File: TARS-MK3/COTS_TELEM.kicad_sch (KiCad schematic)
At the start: 18 parts, among them J1 Conn_02x12_Odd_Even, J2 Conn_02x12_Odd_Even, J3 Conn_02x12_Odd_Even, J4 Conn_02x12_Odd_Even, J5 Conn_01x05_Male, U1 RFM96W-433S2, U2 Feather_M0_RFM96, X1 uFL/SMA

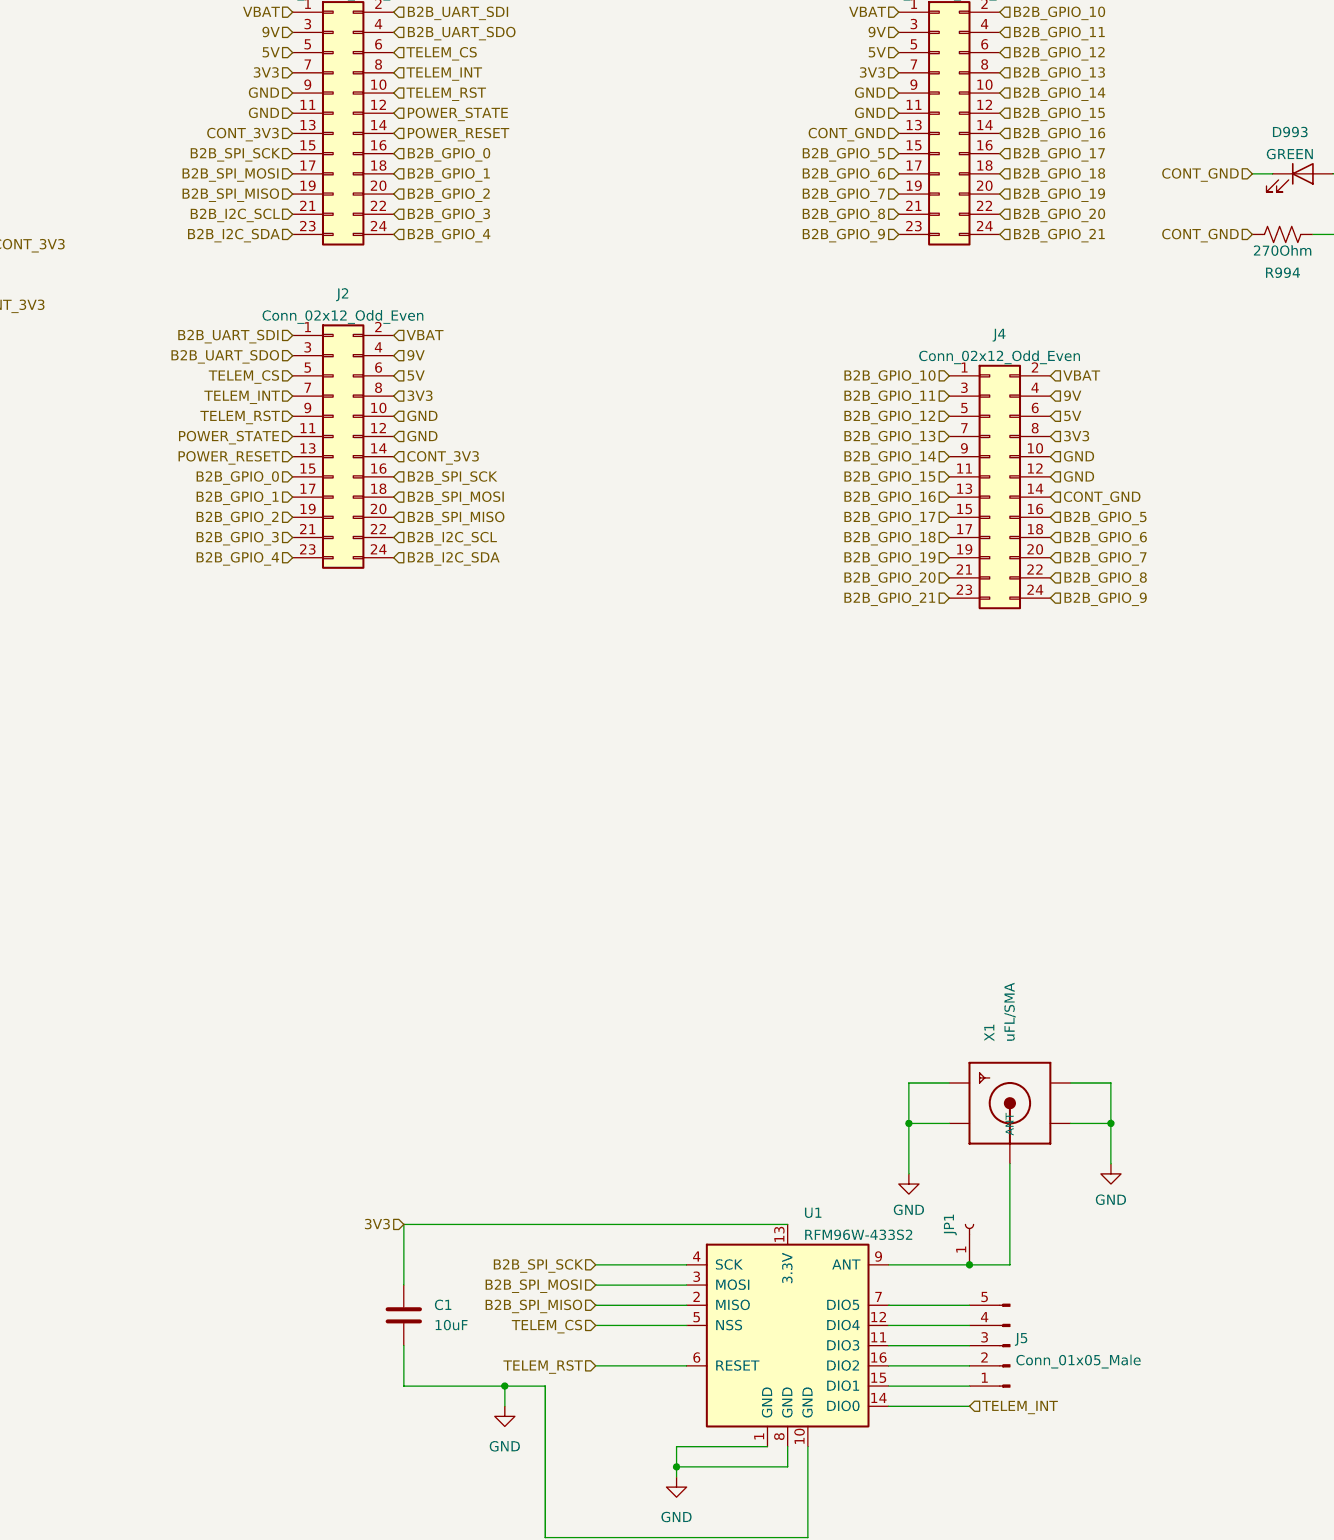
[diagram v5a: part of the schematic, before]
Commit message: allocated telemetry b2b and added battery connector
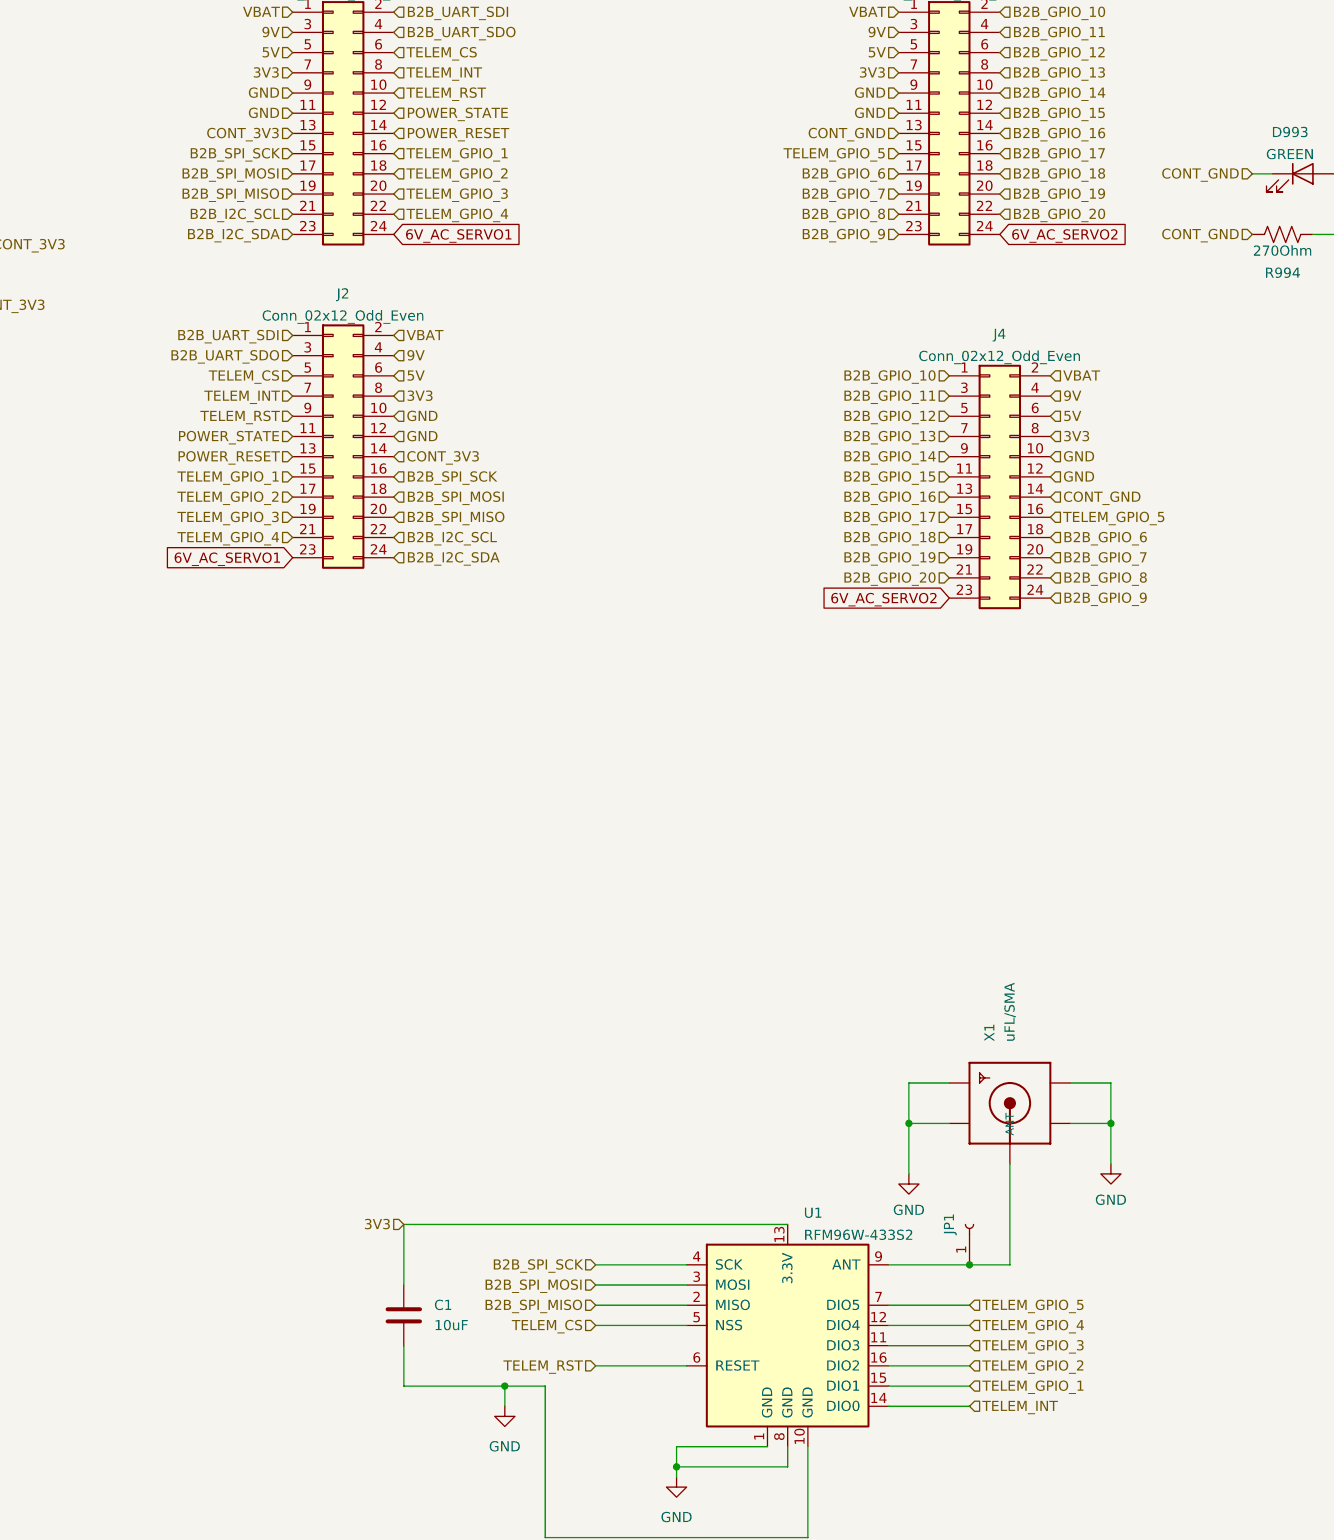
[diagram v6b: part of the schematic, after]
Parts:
- removed J5: Conn_01x05_Male, Connector_PinHeader_2.54mm:PinHeader_1x05_P2.54mm_Vertical, symbol Connector:Conn_01x05_Male
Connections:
- net B2B_GPIO_0 is gone; now on net TELEM_GPIO_1: J1.16 (Pin_16), J2.15 (Pin_15)
- net B2B_GPIO_1 is gone; now on net TELEM_GPIO_2: J1.18 (Pin_18), J2.17 (Pin_17)
- net B2B_GPIO_2 is gone; now on net TELEM_GPIO_3: J1.20 (Pin_20), J2.19 (Pin_19)
- net B2B_GPIO_3 is gone; now on net TELEM_GPIO_4: J1.22 (Pin_22), J2.21 (Pin_21)
- net B2B_GPIO_5 is gone; now on net TELEM_GPIO_5: J3.15 (Pin_15), J4.16 (Pin_16)
- net TELEM_GPIO_1: now reaches U1.15 (DIO1)
- net TELEM_GPIO_2: now reaches U1.16 (DIO2)
- net TELEM_GPIO_3: now reaches U1.11 (DIO3)
- net TELEM_GPIO_4: now reaches U1.12 (DIO4)
- net TELEM_GPIO_5: now reaches U1.7 (DIO5)
- net B2B_GPIO_21 renamed 6V_AC_SERVO2
- net B2B_GPIO_4 renamed 6V_AC_SERVO1

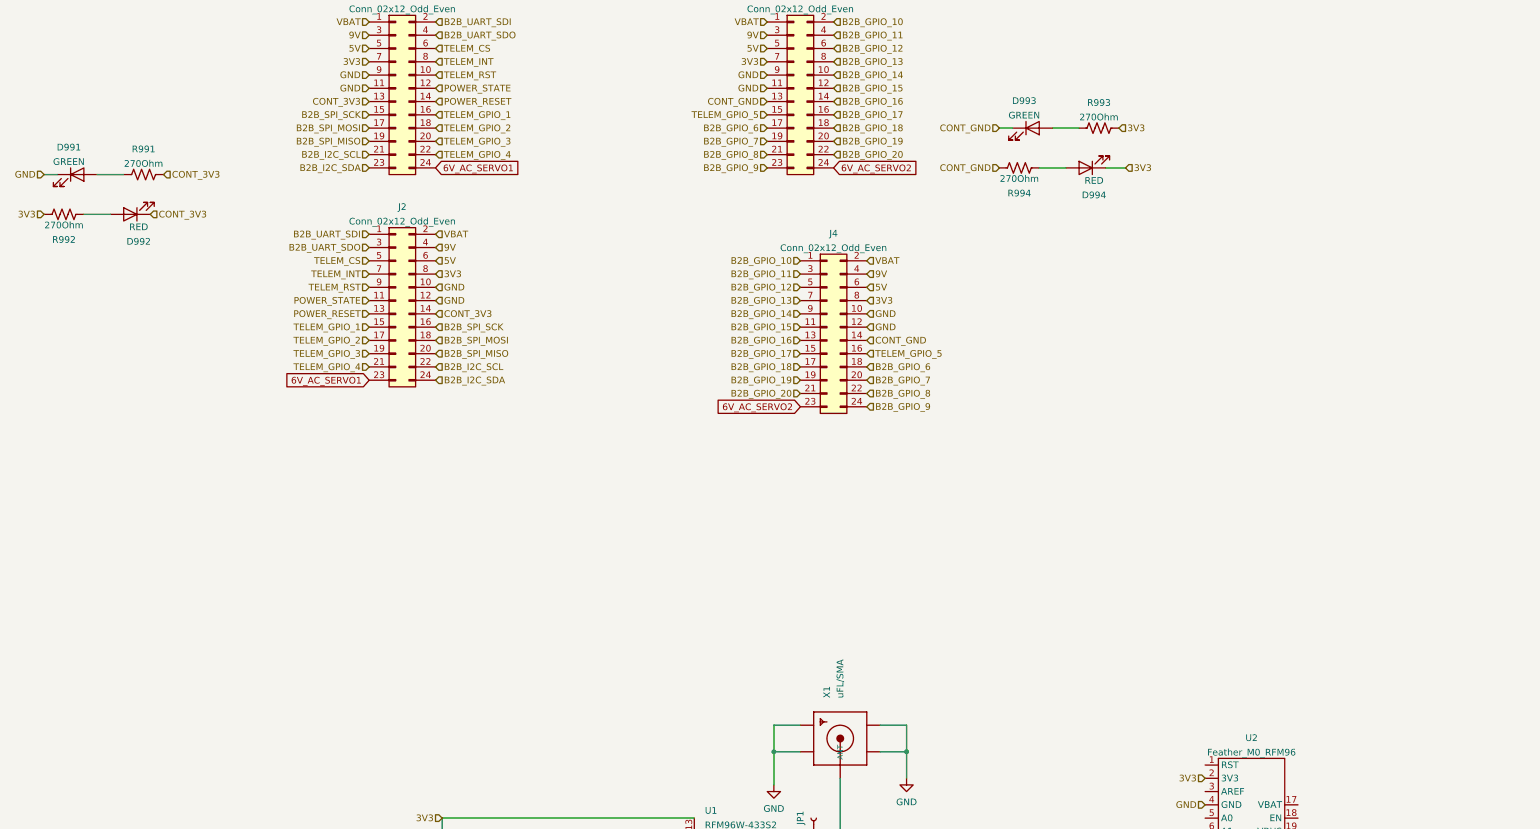
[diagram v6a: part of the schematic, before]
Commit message: moved connectors to top
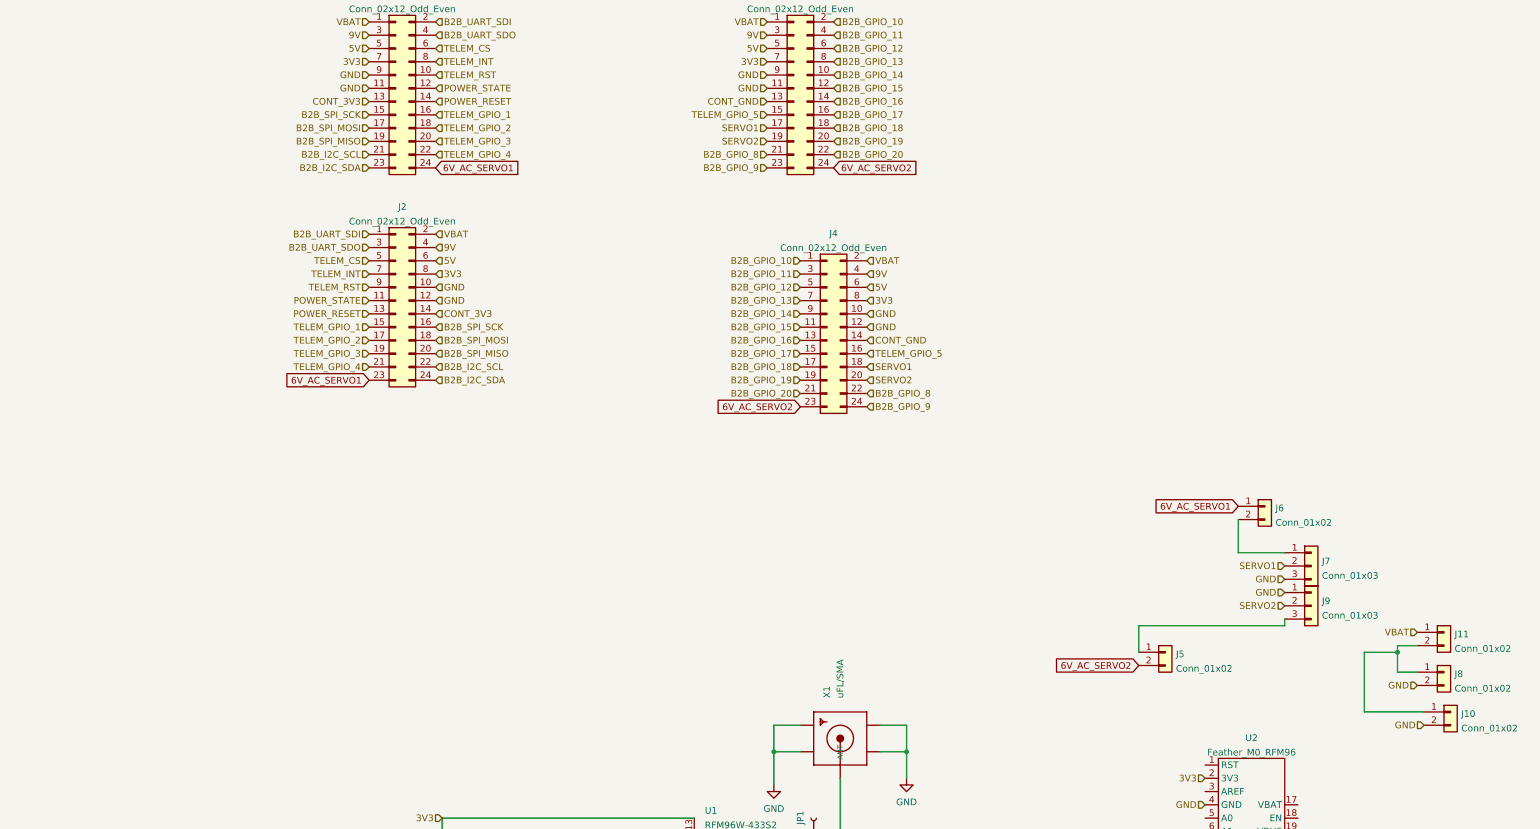
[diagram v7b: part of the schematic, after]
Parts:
- removed D991, D993: GREEN, LED_SMD:LED_0805_2012Metric, symbol D24V50F5:LED
- removed D992, D994: RED, LED_SMD:LED_0805_2012Metric, symbol D24V50F5:LED
- removed R991, R992, R993, R994: 270Ohm, Resistor_SMD:R_0805_2012Metric, symbol D24V50F5:R_US
- added J10, J8: Conn_01x02, Connector_Molex:Molex_Micro-Fit_3.0_43650-0200_1x02_P3.00mm_Horizontal, symbol Connector_Generic:Conn_01x02
- added J11, J5, J6: Conn_01x02, Connector_Molex:Molex_CLIK-Mate_502443-0270_1x02-1MP_P2.00mm_Vertical, symbol Connector_Generic:Conn_01x02
- added J7, J9: Conn_01x03, Connector_Molex:Molex_Micro-Fit_3.0_43650-0300_1x03_P3.00mm_Horizontal, symbol Connector_Generic:Conn_01x03
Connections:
- net 6V_AC_SERVO1: now also J6.1 (Pin_1)
- net 6V_AC_SERVO2: now also J5.2 (Pin_2)
- net GND: now also J10.2 (Pin_2), J7.3 (Pin_3), J8.2 (Pin_2), J9.1 (Pin_1)
- net VBAT: now also J11.1 (Pin_1)
- net B2B_GPIO_6 renamed SERVO1
- net SERVO1: now also J7.2 (Pin_2)
- net B2B_GPIO_7 renamed SERVO2
- net SERVO2: now also J9.2 (Pin_2)
- new net: J6.2 (Pin_2), J7.1 (Pin_1)
- new net: J10.1 (Pin_1), J11.2 (Pin_2), J8.1 (Pin_1)
- new net: J5.1 (Pin_1), J9.3 (Pin_3)

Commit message: stuff
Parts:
- removed J5, J6: Conn_01x02, Connector_Molex:Molex_CLIK-Mate_502443-0270_1x02-1MP_P2.00mm_Vertical, symbol Connector_Generic:Conn_01x02
- J11: footprint Connector_Molex:Molex_CLIK-Mate_502443-0270_1x02-1MP_P2.00mm_Vertical -> Connector_Molex:Molex_CLIK-Mate_502494-0270_1x02-1MP_P2.00mm_Horizontal
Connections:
- net 6V_AC_SERVO1: now also J7.1 (Pin_1)
- net 6V_AC_SERVO2: now also J9.3 (Pin_3)
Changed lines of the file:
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@@
-    (stroke (width 0) (type default) (color 0 0 0 0))
-  )
-  (wire (pts (xy 185.42 44.45) (xy 185.42 39.37))
     (stroke (width 0) (type default) (color 0 0 0 0))
   )
@@
     (stroke (width 0) (type default) (color 0 0 0 0))
   )
-  (wire (pts (xy 204.47 19.05) (xy 204.47 25.4))
-    (stroke (width 0) (type default) (color 0 0 0 0))
-  )
   (wire (pts (xy 234.95 48.26) (xy 238.76 48.26))
     (stroke (width 0) (type default) (color 0 0 0 0))
@@
     (stroke (width 0) (type default) (color 0 0 0 0))
   )
-  (wire (pts (xy 213.36 39.37) (xy 213.36 38.1))
-    (stroke (width 0) (type default) (color 0 0 0 0))
-  )
   (wire (pts (xy 240.03 55.88) (xy 228.6 55.88))
     (stroke (width 0) (type default) (color 0 0 0 0))
@@
     (stroke (width 0) (type default) (color 0 0 0 0))
   )
-  (wire (pts (xy 204.47 25.4) (xy 213.36 25.4))
-    (stroke (width 0) (type default) (color 0 0 0 0))
-  )
   (wire (pts (xy 234.95 43.18) (xy 234.95 44.45))
-    (stroke (width 0) (type default) (color 0 0 0 0))
-  )
-  (wire (pts (xy 185.42 39.37) (xy 213.36 39.37))
     (stroke (width 0) (type default) (color 0 0 0 0))
   )
@@
     )
   )
-  (global_label "6V_AC_SERVO1" (shape input) (at 204.47 16.51 180) (fields_autoplaced)
-    (effects (font (size 1.27 1.27)) (justify right))
-    (property "Intersheet References" "${INTERSHEET_REFS}" (id 0) (at 188.2968 16.4306 0)
+  (global_label "6V_AC_SERVO1" (shape input) (at 213.36 25.4 180) (fields_autoplaced)
+    (effects (font (size 1.27 1.27)) (justify right))
+    (property "Intersheet References" "${INTERSHEET_REFS}" (id 0) (at 197.1868 25.3206 0)
       (effects (font (size 1.27 1.27)) (justify right) hide)
     )
@@
     )
   )
-  (global_label "6V_AC_SERVO2" (shape input) (at 185.42 46.99 180) (fields_autoplaced)
-    (effects (font (size 1.27 1.27)) (justify right))
-    (property "Intersheet References" "${INTERSHEET_REFS}" (id 0) (at 169.2468 46.9106 0)
+  (global_label "6V_AC_SERVO2" (shape input) (at 213.36 38.1 180) (fields_autoplaced)
+    (effects (font (size 1.27 1.27)) (justify right))
+    (property "Intersheet References" "${INTERSHEET_REFS}" (id 0) (at 197.1868 38.0206 0)
       (effects (font (size 1.27 1.27)) (justify right) hide)
     )
@@
     (pin "2")
   )
-  (symbol (lib_id "Connector_Generic:Conn_01x02") (at 190.5 44.45 0) (unit 1)
-    (in_bom yes) (on_board yes) (fields_autoplaced)
-    (property "Reference" "J5" (id 0) (at 192.532 44.8115 0)
-      (effects (font (size 1.27 1.27)) (justify left))
-    )
-    (property "Value" "Conn_01x02" (id 1) (at 192.532 47.5866 0)
-      (effects (font (size 1.27 1.27)) (justify left))
-    )
-    (property "Footprint" "Connector_Molex:Molex_CLIK-Mate_502443-0270_1x02-1MP_P2.00mm_Vertical" (id 2) (at 190.5 44.45 0)
-      (effects (font (size 1.27 1.27)) hide)
-    )
-    (property "Datasheet" "~" (id 3) (at 190.5 44.45 0)
-      (effects (font (size 1.27 1.27)) hide)
-    )
-    (pin "1")
-    (pin "2")
-  )
   (symbol (lib_id "Connector_Generic:Conn_02x12_Odd_Even") (at 43.18 -22.86 0) (unit 1)
     (in_bom yes) (on_board yes) (fields_autoplaced)
@@
     (pin "9")
   )
-  (symbol (lib_id "Connector_Generic:Conn_01x02") (at 209.55 16.51 0) (unit 1)
-    (in_bom yes) (on_board yes) (fields_autoplaced)
-    (property "Reference" "J6" (id 0) (at 211.582 16.8715 0)
-      (effects (font (size 1.27 1.27)) (justify left))
-    )
-    (property "Value" "Conn_01x02" (id 1) (at 211.582 19.6466 0)
-      (effects (font (size 1.27 1.27)) (justify left))
-    )
-    (property "Footprint" "Connector_Molex:Molex_CLIK-Mate_502443-0270_1x02-1MP_P2.00mm_Vertical" (id 2) (at 209.55 16.51 0)
-      (effects (font (size 1.27 1.27)) hide)
-    )
-    (property "Datasheet" "~" (id 3) (at 209.55 16.51 0)
-      (effects (font (size 1.27 1.27)) hide)
-    )
-    (pin "1")
-    (pin "2")
-  )
   (symbol (lib_id "Connector_Generic:Conn_01x02") (at 243.84 40.64 0) (unit 1)
     (in_bom yes) (on_board yes) (fields_autoplaced)
@@
       (effects (font (size 1.27 1.27)) (justify left))
     )
-    (property "Footprint" "Connector_Molex:Molex_CLIK-Mate_502443-0270_1x02-1MP_P2.00mm_Vertical" (id 2) (at 243.84 40.64 0)
+    (property "Footprint" "Connector_Molex:Molex_CLIK-Mate_502494-0270_1x02-1MP_P2.00mm_Horizontal" (id 2) (at 243.84 40.64 0)
       (effects (font (size 1.27 1.27)) hide)
     )
@@
       (reference "J4") (unit 1) (value "Conn_02x12_Odd_Even") (footprint "Connector_PinHeader_2.54mm:PinHeader_2x12_P2.54mm_Vertical_SMD")
     )
-    (path "/d3f763e6-13d5-4205-adb1-a12fd2c8df82"
-      (reference "J5") (unit 1) (value "Conn_01x02") (footprint "Connector_Molex:Molex_CLIK-Mate_502443-0270_1x02-1MP_P2.00mm_Vertical")
-    )
-    (path "/e9220e2d-ac28-4d78-9b4e-95f156910763"
-      (reference "J6") (unit 1) (value "Conn_01x02") (footprint "Connector_Molex:Molex_CLIK-Mate_502443-0270_1x02-1MP_P2.00mm_Vertical")
-    )
     (path "/6194a47f-48bf-4d66-984b-72fa571e177b"
       (reference "J7") (unit 1) (value "Conn_01x03") (footprint "Connector_Molex:Molex_Micro-Fit_3.0_43650-0300_1x03_P3.00mm_Horizontal")
@@
     )
     (path "/eb62d39d-6f37-46b8-9c1d-ed974a0a8b66"
-      (reference "J11") (unit 1) (value "Conn_01x02") (footprint "Connector_Molex:Molex_CLIK-Mate_502443-0270_1x02-1MP_P2.00mm_Vertical")
+      (reference "J11") (unit 1) (value "Conn_01x02") (footprint "Connector_Molex:Molex_CLIK-Mate_502494-0270_1x02-1MP_P2.00mm_Horizontal")
     )
     (path "/7b292ab1-954a-4e1e-9491-c38a40018cab"
